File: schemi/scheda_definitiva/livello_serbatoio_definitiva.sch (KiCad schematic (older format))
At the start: 36 parts, among them J1 USB_B, J2 CONN_US, J3 CONN_LCD, J4 BTN_LED_GROUP, J5 Conn_01x06_Male, SW1 SW_RST, U1 FT232RL, U2 ATmega328P-PU, Y1 16MHz

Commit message: spostati componenti e fatto nuovo sbroglio
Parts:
- removed F1: 500mA, Fuse:Fuse_Littelfuse-LVR100, symbol Device:Fuse
- removed J5: Conn_01x06_Male, Connector_PinHeader_2.54mm:PinHeader_1x06_P2.54mm_Horizontal, symbol Connector:Conn_01x06_Male
- added FB1: MF-MSMF050-2, Inductor_SMD:L_1812_4532Metric_Pad1.30x3.40mm_HandSolder, symbol Device:Ferrite_Bead
- added J5: ICSP, Connector_PinHeader_2.54mm:PinHeader_2x03_P2.54mm_Vertical, symbol Connector_Generic:Conn_02x03_Odd_Even
- C1, C2, C3, C4, C6, C7, C8: footprint Capacitor_THT:C_Axial_L3.8mm_D2.6mm_P7.50mm_Horizontal -> Capacitor_THT:C_Radial_D5.0mm_H5.0mm_P2.00mm
- J1: footprint Connector_USB:USB_B_OST_USB-B1HSxx_Horizontal -> simboli_custom:USB_B_OST_USB-B1HSxx_Horizontal; symbol Connector:USB_B -> livello_serbatoio_definitiva-rescue:USB_B-Connector
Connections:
- net D11: now also J5.4 (Pin_4)
- net D12: now also J5.1 (Pin_1)
- net D13: now also J5.3 (Pin_3)
- net GND: now also J5.6 (Pin_6)
- net ICSP_RST: now also J5.5 (Pin_5)
- net VCC: now also FB1.1, J5.2 (Pin_2)
- net X2: now reaches C8.2, R7.2, U2.10 (XTAL2/PB7), Y1.1
- net X1: now reaches C7.2, R7.1, U2.9 (XTAL1/PB6), Y1.2
- net at C1.1, J1.1 (VBUS): now also FB1.2
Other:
- moved on the sheet: C2
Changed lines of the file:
@@
-$EndComp
-$Comp
-L Connector:USB_B J1
-U 1 1 5F0BA65A
-P 950 2950
-F 0 "J1" H 1007 3417 50  0000 C CNN
-F 1 "USB_B" H 1007 3326 50  0000 C CNN
-F 2 "Connector_USB:USB_B_OST_USB-B1HSxx_Horizontal" H 1100 2900 50  0001 C CNN
-F 3 " ~" H 1100 2900 50  0001 C CNN
-	1    950  2950
-	1    0    0    -1
 $EndComp
 $Comp
@@
 F 0 "C7" V 7750 2700 50  0000 C CNN
 F 1 "22pF" V 7639 2600 50  0000 C CNN
-F 2 "Capacitor_THT:C_Axial_L3.8mm_D2.6mm_P7.50mm_Horizontal" H 7838 2450 50  0001 C CNN
+F 2 "Capacitor_THT:C_Radial_D5.0mm_H5.0mm_P2.00mm" H 7838 2450 50  0001 C CNN
 F 3 "~" H 7800 2600 50  0001 C CNN
 	1    7800 2600
@@
 F 0 "C8" V 7850 3150 50  0000 C CNN
 F 1 "22pF" V 7950 3050 50  0000 C CNN
-F 2 "Capacitor_THT:C_Axial_L3.8mm_D2.6mm_P7.50mm_Horizontal" H 7838 2900 50  0001 C CNN
+F 2 "Capacitor_THT:C_Radial_D5.0mm_H5.0mm_P2.00mm" H 7838 2900 50  0001 C CNN
 F 3 "~" H 7800 3050 50  0001 C CNN
 	1    7800 3050
@@
 F 0 "C4" V 2748 5700 50  0000 C CNN
 F 1 "100nF" V 2839 5700 50  0000 C CNN
-F 2 "Capacitor_THT:C_Axial_L3.8mm_D2.6mm_P7.50mm_Horizontal" H 3038 5550 50  0001 C CNN
+F 2 "Capacitor_THT:C_Radial_D5.0mm_H5.0mm_P2.00mm" H 3038 5550 50  0001 C CNN
 F 3 "~" H 3000 5700 50  0001 C CNN
 	1    3000 5700
@@
 F 0 "C3" H 5300 1900 50  0000 C CNN
 F 1 "100nF" V 5500 2000 50  0000 C CNN
-F 2 "Capacitor_THT:C_Axial_L3.8mm_D2.6mm_P7.50mm_Horizontal" H 5388 1850 50  0001 C CNN
+F 2 "Capacitor_THT:C_Radial_D5.0mm_H5.0mm_P2.00mm" H 5388 1850 50  0001 C CNN
 F 3 "~" H 5350 2000 50  0001 C CNN
 	1    5350 2000
@@
 F 0 "C6" V 6700 1700 50  0000 C CNN
 F 1 "100nF" V 6600 1700 50  0000 C CNN
-F 2 "Capacitor_THT:C_Axial_L3.8mm_D2.6mm_P7.50mm_Horizontal" H 6488 1550 50  0001 C CNN
+F 2 "Capacitor_THT:C_Radial_D5.0mm_H5.0mm_P2.00mm" H 6488 1550 50  0001 C CNN
 F 3 "~" H 6450 1700 50  0001 C CNN
 	1    6450 1700
@@
 Wire Wire Line
 	3050 4350 3050 4550
-Wire Wire Line
-	850  3350 850  3400
-Wire Wire Line
-	850  3400 950  3400
-Connection ~ 950  3400
 Connection ~ 2250 4350
 Wire Wire Line
@@
 F 0 "C1" H 1415 3546 50  0000 L CNN
 F 1 "100nF" H 1415 3455 50  0000 L CNN
-F 2 "Capacitor_THT:C_Axial_L3.8mm_D2.6mm_P7.50mm_Horizontal" H 1338 3350 50  0001 C CNN
+F 2 "Capacitor_THT:C_Radial_D5.0mm_H5.0mm_P2.00mm" H 1338 3350 50  0001 C CNN
 F 3 "~" H 1300 3500 50  0001 C CNN
 	1    1300 3500
@@
 L Device:C C2
 U 1 1 5F19380D
-P 1750 3500
-F 0 "C2" H 1865 3546 50  0000 L CNN
-F 1 "100nF" H 1865 3455 50  0000 L CNN
-F 2 "Capacitor_THT:C_Axial_L3.8mm_D2.6mm_P7.50mm_Horizontal" H 1788 3350 50  0001 C CNN
-F 3 "~" H 1750 3500 50  0001 C CNN
-	1    1750 3500
-	1    0    0    -1
-$EndComp
-Wire Wire Line
-	2250 2650 1750 2650
-Wire Wire Line
-	1750 2650 1750 3350
-Wire Wire Line
-	1750 3650 1300 3650
-Connection ~ 1300 3650
+P 2100 2650
+F 0 "C2" V 1950 2600 50  0000 L CNN
+F 1 "100nF" V 2250 2550 50  0000 L CNN
+F 2 "Capacitor_THT:C_Radial_D5.0mm_H5.0mm_P2.00mm" H 2138 2500 50  0001 C CNN
+F 3 "~" H 2100 2650 50  0001 C CNN
+	1    2100 2650
+	0    1    1    0
+$EndComp
 Wire Wire Line
 	1300 2350 1350 2350
@@
 Wire Wire Line
 	2150 2150 2150 2350
-$Comp
-L Device:Fuse F1
-U 1 1 5F1C7FD2
-P 1500 2350
-F 0 "F1" V 1303 2350 50  0000 C CNN
-F 1 "500mA" V 1394 2350 50  0000 C CNN
-F 2 "Fuse:Fuse_Littelfuse-LVR100" V 1430 2350 50  0001 C CNN
-F 3 "~" H 1500 2350 50  0001 C CNN
-	1    1500 2350
-	0    1    1    0
-$EndComp
 Wire Wire Line
 	1650 2350 2150 2350
@@
 Wire Wire Line
 	4350 3750 4300 3750
-Connection ~ 850  3400
-Wire Wire Line
-	850  3400 850  3450
 Connection ~ 1300 2750
 Wire Wire Line
 	1300 2750 1300 3350
-Wire Wire Line
-	950  3400 950  3350
-Wire Wire Line
-	950  3400 950  3650
 Wire Wire Line
 	1300 2350 1300 2750
@@
 	11000 800  11000 1800
 Wire Notes Line
-	750  1800 5000 1800
-Wire Notes Line
 	5000 1800 5000 6850
 Wire Notes Line
@@
 Wire Notes Line
 	650  6850 650  1800
-Wire Notes Line
-	650  1800 700  1800
 Text Notes 2550 1950 0    50   ~ 0
 USB Programmer
@@
 Text Notes 6350 5450 0    50   ~ 0
 ICSP - Bootloader
-$Comp
-L Connector:Conn_01x06_Male J5
-U 1 1 5F49926C
-P 7150 5900
-F 0 "J5" H 7122 5782 50  0000 R CNN
-F 1 "Conn_01x06_Male" H 7550 6200 50  0000 R CNN
-F 2 "Connector_PinHeader_2.54mm:PinHeader_1x06_P2.54mm_Horizontal" H 7150 5900 50  0001 C CNN
-F 3 "~" H 7150 5900 50  0001 C CNN
-	1    7150 5900
-	-1   0    0    1
-$EndComp
-Text GLabel 6550 5900 0    50   Input ~ 0
+Text GLabel 6350 5850 0    50   Input ~ 0
 ICSP_MISO
-Text GLabel 6550 6100 0    50   Input ~ 0
+Text GLabel 7300 5950 2    50   Input ~ 0
 ICSP_MOSI
 $Comp
 L power:VCC #PWR017
 U 1 1 5F4B97E7
-P 6550 6000
-F 0 "#PWR017" H 6550 5850 50  0001 C CNN
-F 1 "VCC" V 6565 6127 50  0000 L CNN
-F 2 "" H 6550 6000 50  0001 C CNN
-F 3 "" H 6550 6000 50  0001 C CNN
-	1    6550 6000
-	0    -1   -1   0
-$EndComp
-Text GLabel 6550 5800 0    50   Input ~ 0
+P 7300 5850
+F 0 "#PWR017" H 7300 5700 50  0001 C CNN
+F 1 "VCC" V 7315 5977 50  0000 L CNN
+F 2 "" H 7300 5850 50  0001 C CNN
+F 3 "" H 7300 5850 50  0001 C CNN
+	1    7300 5850
+	1    0    0    -1
+$EndComp
+Text GLabel 6350 5950 0    50   Input ~ 0
 ICSP_SCK
-Text GLabel 6550 5700 0    50   Input ~ 0
+Text GLabel 6350 6050 0    50   Input ~ 0
 ICSP_RST
 $Comp
 L power:GND #PWR07
 U 1 1 5F4BAD5C
-P 6550 5600
-F 0 "#PWR07" H 6550 5350 50  0001 C CNN
-F 1 "GND" V 6555 5472 50  0000 R CNN
-F 2 "" H 6550 5600 50  0001 C CNN
-F 3 "" H 6550 5600 50  0001 C CNN
-	1    6550 5600
-	0    1    1    0
-$EndComp
-Wire Wire Line
-	6550 5600 6950 5600
-Wire Wire Line
-	6550 5700 6950 5700
-Wire Wire Line
-	6550 5800 6950 5800
-Wire Wire Line
-	6550 5900 6950 5900
-Wire Wire Line
-	6550 6000 6950 6000
-Wire Wire Line
-	6550 6100 6950 6100
+P 7300 6050
+F 0 "#PWR07" H 7300 5800 50  0001 C CNN
+F 1 "GND" V 7305 5922 50  0000 R CNN
+F 2 "" H 7300 6050 50  0001 C CNN
+F 3 "" H 7300 6050 50  0001 C CNN
+	1    7300 6050
+	1    0    0    -1
+$EndComp
 Text GLabel 7100 2350 2    50   Output ~ 0
 ICSP_MISO
@@
 L power:GND #PWR022
 U 1 1 5F5C8BD6
-P 3050 1300
-F 0 "#PWR022" H 3050 1050 50  0001 C CNN
-F 1 "GND" H 3055 1127 50  0000 C CNN
-F 2 "" H 3050 1300 50  0001 C CNN
-F 3 "" H 3050 1300 50  0001 C CNN
-	1    3050 1300
+P 3050 1150
+F 0 "#PWR022" H 3050 900 50  0001 C CNN
+F 1 "GND" H 3055 977 50  0000 C CNN
+F 2 "" H 3050 1150 50  0001 C CNN
+F 3 "" H 3050 1150 50  0001 C CNN
+	1    3050 1150
 	1    0    0    -1
 $EndComp
@@
 	2500 1100 2850 1100
 Wire Wire Line
-	2850 1100 3200 1100
+	2850 1100 3050 1100
 Connection ~ 2850 1100
 Wire Wire Line
 	3200 1100 3550 1100
 Connection ~ 3200 1100
-Wire Wire Line
-	3200 1100 3200 1150
-Wire Wire Line
-	3200 1150 3050 1150
-Wire Wire Line
-	3050 1150 3050 1300
 $Comp
 L MCU_Microchip_ATmega:ATmega328P-PU U2
@@
 Text Label 1500 3050 0    50   ~ 0
 D-
+Text Label 3650 2350 0    50   ~ 0
++5V
+Text Label 1700 4350 0    50   ~ 0
+GND
+Text Label 7300 2650 0    50   ~ 0
+X1
+Text Label 7300 2950 0    50   ~ 0
+X2
+Wire Wire Line
+	3050 1150 3050 1100
+Connection ~ 3050 1100
+Wire Wire Line
+	3050 1100 3200 1100
+$Comp
+L Device:Ferrite_Bead FB1
+U 1 1 5F8E145F
+P 1500 2350
+F 0 "FB1" V 1350 2350 50  0000 C CNN
+F 1 "MF-MSMF050-2" V 1650 2500 50  0000 C CNN
+F 2 "Inductor_SMD:L_1812_4532Metric_Pad1.30x3.40mm_HandSolder" V 1430 2350 50  0001 C CNN
+F 3 "~" H 1500 2350 50  0001 C CNN
+	1    1500 2350
+	0    1    1    0
+$EndComp
+$Comp
+L power:GND #PWR023
+U 1 1 5F8EF1F8
+P 1950 2650
+F 0 "#PWR023" H 1950 2400 50  0001 C CNN
+F 1 "GND" H 1955 2477 50  0000 C CNN
+F 2 "" H 1950 2650 50  0001 C CNN
+F 3 "" H 1950 2650 50  0001 C CNN
+	1    1950 2650
+	1    0    0    -1
+$EndComp
+Wire Wire Line
+	950  3350 950  3650
+Wire Notes Line
+	650  1800 5000 1800
+$Comp
+L livello_serbatoio_definitiva-rescue:USB_B-Connector J1
+U 1 1 5F0BA65A
+P 950 2950
+F 0 "J1" H 1007 3417 50  0000 C CNN
+F 1 "USB_B" H 1007 3326 50  0000 C CNN
+F 2 "simboli_custom:USB_B_OST_USB-B1HSxx_Horizontal" H 1100 2900 50  0001 C CNN
+F 3 " ~" H 1100 2900 50  0001 C CNN
+	1    950  2950
+	1    0    0    -1
+$EndComp
+Wire Wire Line
+	850  3350 950  3350
+Connection ~ 950  3350
+Text Label 10600 5650 0    50   ~ 0
+GND
+$Comp
+L Connector_Generic:Conn_02x03_Odd_Even J5
+U 1 1 5F8DF7DB
+P 6750 5950
+F 0 "J5" H 6800 6267 50  0000 C CNN
+F 1 "ICSP" H 6800 6176 50  0000 C CNN
+F 2 "Connector_PinHeader_2.54mm:PinHeader_2x03_P2.54mm_Vertical" H 6750 5950 50  0001 C CNN
+F 3 "~" H 6750 5950 50  0001 C CNN
+	1    6750 5950
+	1    0    0    -1
+$EndComp
+Wire Wire Line
+	6350 5850 6550 5850
+Wire Wire Line
+	6350 5950 6550 5950
+Wire Wire Line
+	6350 6050 6550 6050
+Wire Wire Line
+	7050 5850 7300 5850
+Wire Wire Line
+	7050 5950 7300 5950
+Wire Wire Line
+	7050 6050 7300 6050
 $EndSCHEMATC

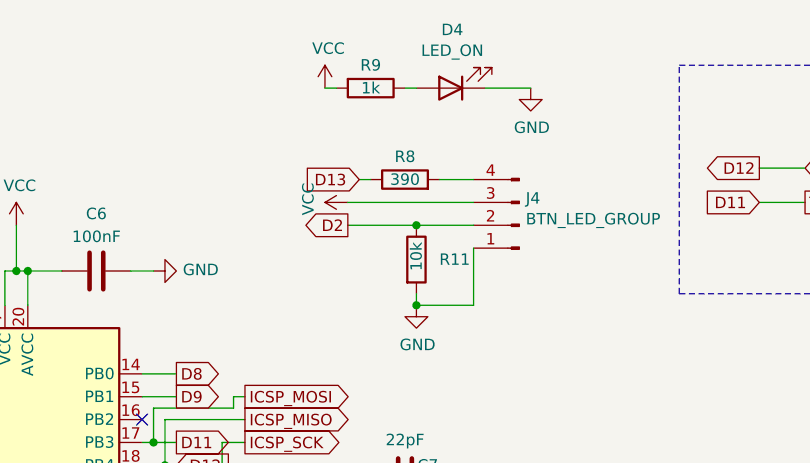
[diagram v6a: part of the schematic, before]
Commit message: nuovo routing + BOM + aggiornamento lista componenti
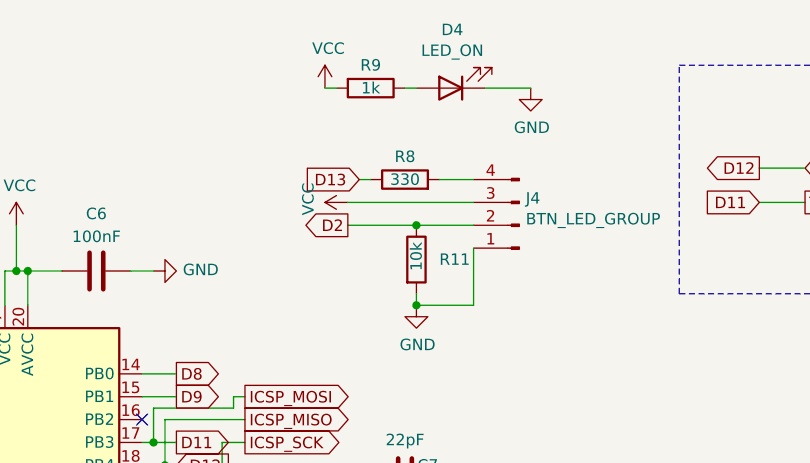
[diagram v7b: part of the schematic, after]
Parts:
- R8: value 390 -> 330
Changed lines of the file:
@@
 P 7800 1300
 F 0 "R8" V 7900 1300 50  0000 C CNN
-F 1 "390" V 7800 1300 50  0000 C CNN
+F 1 "330" V 7800 1300 50  0000 C CNN
 F 2 "Resistor_THT:R_Axial_DIN0207_L6.3mm_D2.5mm_P7.62mm_Horizontal" V 7730 1300 50  0001 C CNN
 F 3 "~" H 7800 1300 50  0001 C CNN
@@
 Text GLabel 7100 2250 2    50   Output ~ 0
 ICSP_MOSI
-Text GLabel 7100 2450 2    50   Output ~ 0
-ICSP_SCK
-Wire Wire Line
-	7000 2450 7000 2700
-Wire Wire Line
-	7000 2700 6750 2700
 Wire Wire Line
 	6750 2700 6750 2650
-Wire Wire Line
-	7000 2450 7100 2450
 Connection ~ 6750 2650
 Wire Wire Line
@@
 Wire Wire Line
 	7050 6050 7300 6050
+Wire Wire Line
+	7000 2700 6750 2700
+Wire Wire Line
+	7000 2450 7000 2700
+Wire Wire Line
+	7000 2450 7100 2450
+Text GLabel 7100 2450 2    50   Output ~ 0
+ICSP_SCK
 $EndSCHEMATC

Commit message: fix a scheda - corrette footprint (adeguate a componenti in possesso) - nuovo routing e layout scheda - aggiunto logo - aggiornato gerber
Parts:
- removed J2: CONN_US, Connector_Molex:Molex_Micro-Latch_53254-0470_1x04_P2.00mm_Horizontal, symbol Connector:Conn_01x04_Female
- removed J4: BTN_LED_GROUP, Connector_Molex:Molex_Micro-Latch_53254-0470_1x04_P2.00mm_Horizontal, symbol Connector:Conn_01x04_Male
- added J2: BTN_LED_GROUP, simboli_custom:TerminalBlock_RND_205-00047_1x04_P5.00mm_Horizontal, symbol Connector:Screw_Terminal_01x04
- added J4: CONN_US, simboli_custom:TerminalBlock_RND_205-00047_1x04_P5.00mm_Horizontal, symbol Connector:Screw_Terminal_01x04
- C1, C2, C3, C4, C6, C7, C8: footprint Capacitor_THT:C_Radial_D5.0mm_H5.0mm_P2.00mm -> Capacitor_THT:C_Disc_D5.0mm_W2.5mm_P2.50mm
- D1, D2, D4: footprint LED_THT:LED_D3.0mm -> LED_THT:LED_D5.0mm
- R1, R11, R2, R3, R4, R5, R6, R7, R8, R9: footprint Resistor_THT:R_Axial_DIN0207_L6.3mm_D2.5mm_P7.62mm_Horizontal -> Resistor_THT:R_Axial_DIN0309_L9.0mm_D3.2mm_P12.70mm_Horizontal
- RV1: footprint Potentiometer_THT:Potentiometer_Vishay_T73YP_Vertical -> simboli_custom:Trimmer_ACP_470
- SW1: footprint Button_Switch_THT:SW_PUSH_6mm -> Button_Switch_THT:SW_PUSH_6mm_H5mm
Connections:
- net D11: now also J4.2 (Pin_2)
- net D12: now also J4.3 (Pin_3)
- net D2: now also J2.3 (Pin_3)
- net GND: now also J2.4 (Pin_4), J4.4 (Pin_4)
- net VCC: now also J2.2 (Pin_2), J4.1 (Pin_1)
- net at R8.2: now also J2.1 (Pin_1)
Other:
- note added: "BLK"
- note added: "BLK connected to GND\nRW connected to GND\nVSS connected to GND"
- note added: "RW"
- note added: "VSS"
- moved on the sheet: J3, RV1
